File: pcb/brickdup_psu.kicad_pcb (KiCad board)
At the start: 2 copper layers, 32 x 18 mm, 24 parts, among them J1 VBAT/GND in, J2 5V/SENSE/GND, U1 MP9486A

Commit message: pcb: JST-PH connectors (J1/J2) + more LEMO clearance
Switch board I/O to JST-PH 2.0mm SMD side-entry connectors so the board is
plug-in/serviceable and stays single-side SMD for JLC:
- J1 (S2B-PH-SM4-TB): VBAT/GND from the LEMO (crimp cable = no solder).
- J2 (S3B-PH-SM4-TB): 5V/SENSE(GPIO7)/GND to the Heltec (pigtail; the Heltec's
  3 pads remain the one unavoidable solder point since it's a bare module).
Schematic/BOM/outline/render updated; ERC still electrically clean; gerbers OK.
Placement remains a rough GUI-arrange/route starting point.

Enclosure: add psu_gap_e (board east edge holdback) so J1 + its plug clear the
LEMO's rear cups. Clearance echo now reports 15.6 mm (was 12.6). Compiles clean.

Co-Authored-By: Claude Opus 4.8 <noreply@anthropic.com>
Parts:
- J1: value VBAT/GND in -> VBAT/GND (JST PH); footprint PinHeader_1x02_P2.54mm_Vertical -> JST_PH_S2B-PH-SM4-TB_1x02-1MP_P2.00mm_Horizontal
- J2: value 5V/SENSE/GND -> 5V/SENSE/GND (JST PH); footprint PinHeader_1x03_P2.54mm_Vertical -> JST_PH_S3B-PH-SM4-TB_1x03-1MP_P2.00mm_Horizontal
- moved J1 2.55 mm to (28.5, 13.0), turned to -90 degrees
- moved J2 1.58 mm to (6.00, 2.50)

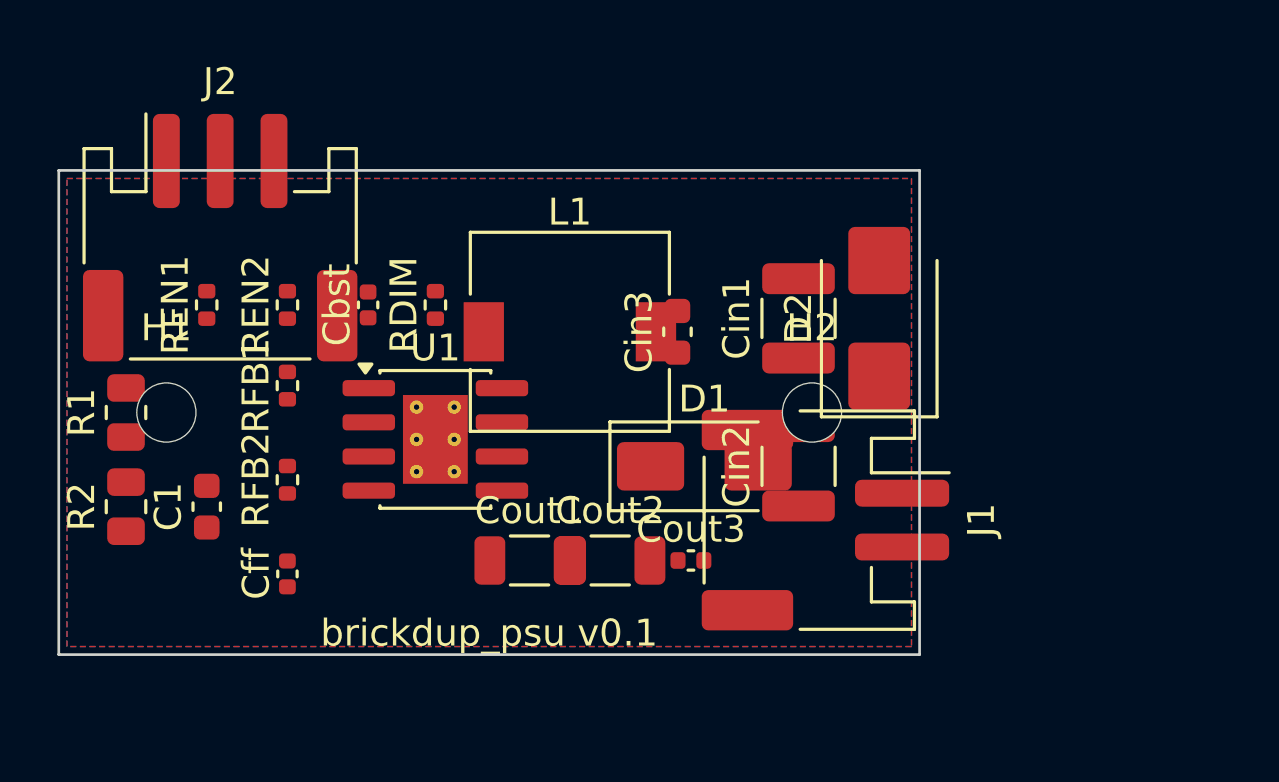
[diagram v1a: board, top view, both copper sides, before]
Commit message: pcb: enlarge board to 38x18 + diagonal corner holes for easier layout
Grow the board length-wise (32 -> 38 mm; width stays 18, set by the south
channel) for ~19% more area to spread parts, and move the two M2 mounting holes
to diagonal corners (NW 4,4 / SE 34,14) so the central band is free for the
regulator + input cluster. Net effect: much easier to arrange + route in the GUI.

Enclosure (node_enclosure.scad v11): psu_l 38, psu_holes as diagonal corner
pairs (bosses + pilots iterate the pair list). Outer box unchanged at
75.6 x 60.7 x 24.4 mm (length grew into the existing channel); LEMO clearance
still 15.6 mm. base/lid/both compile clean.

PCB: re-placed all 22 parts in functional zones using the freed centre; ERC
electrically clean, gerbers export. Placement still a rough GUI starting point.
Board outline SVG + README dims updated to 38x18 / corner holes.

Co-Authored-By: Claude Opus 4.8 <noreply@anthropic.com>
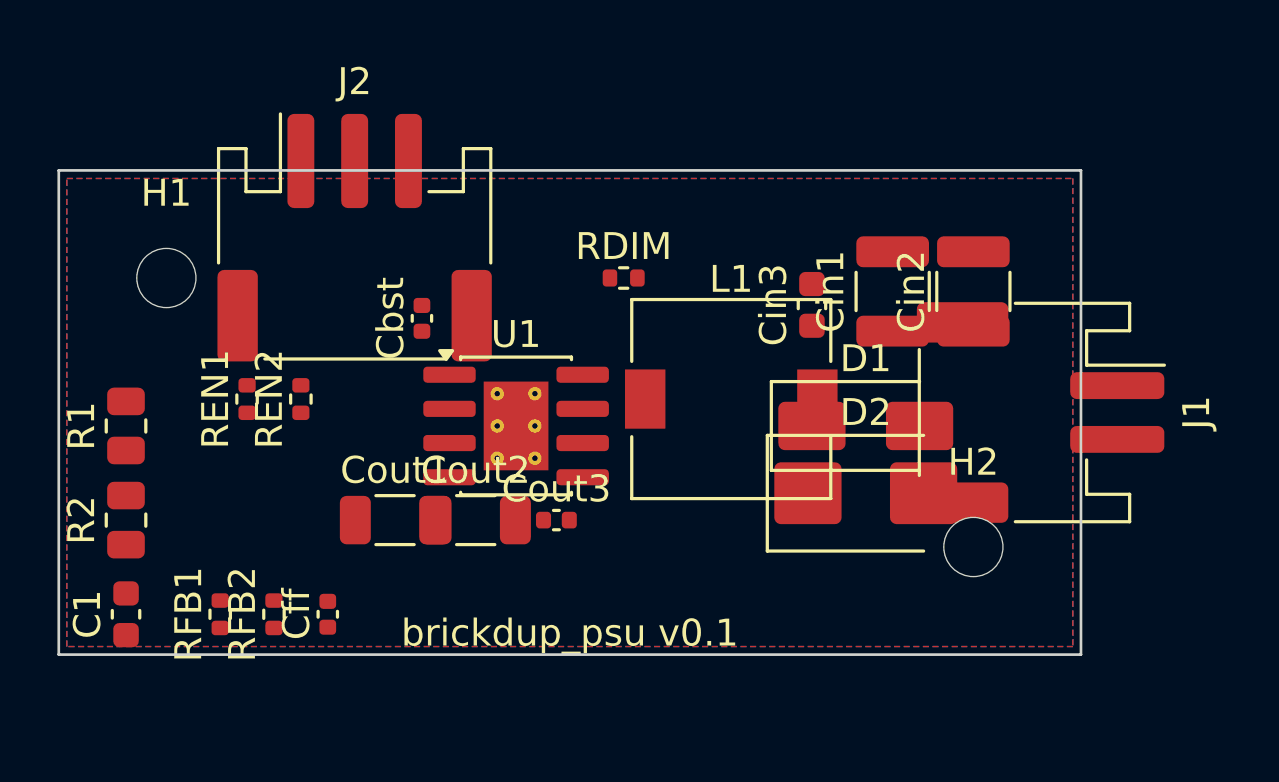
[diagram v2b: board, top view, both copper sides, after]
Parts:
- moved Cin2 9.19 mm to (34.0, 4.50)
- moved J1 8.94 mm to (36.5, 9.00)
- moved RFB1 8.86 mm to (6.00, 16.5)
- moved H2 7.81 mm to (34.0, 14.0)
- moved RDIM 7.07 mm to (21.0, 4.00), turned to 0 degrees
- moved D2 6.52 mm to (30.0, 12.0), turned to 0 degrees
- moved L1 6.50 mm to (25.0, 8.50)
- moved D1 6.18 mm to (30.0, 9.50)
- moved Cout1 5.22 mm to (12.5, 13.0)
- moved Cout2 5.22 mm to (15.5, 13.0)
- moved Cout3 5.22 mm to (18.5, 13.0)
- moved Cin3 5.10 mm to (28.0, 5.00)
- moved RFB2 5.02 mm to (8.00, 16.5)
- moved C1 5.00 mm to (2.50, 16.5)
- moved H1 5.00 mm to (4.00, 4.00)
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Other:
- board size 32 x 18 mm -> 38 x 18 mm

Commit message: pcb: 40x20 board + auto-spread placement (0 pad overlaps)
Enlarge to 40x20 mm and add a separation-solver placement (random-restart
relaxation using pad-bbox extents) that reaches 0 pad overlaps -- a clean,
manufacturable, routable starting board (previously parts sat on each other /
on the mounting holes). Mounting holes diagonal at (4,4) and (32,16); the SE
hole is pulled inboard so it clears the east-edge J1 connector. GND pours both
layers; value silk hidden, refs shrunk.

Enclosure v11: psu_l 40, psu_w 20, psu_holes (4,4)+(32,16). Outer grows to
~76 x 63 x 24 mm; LEMO clearance 15.1 mm. Compiles clean.

Routing is still to do (the 41 unconnected DRC items are the ratsnest). Docs +
board_outline.svg updated to 40x20.

Co-Authored-By: Claude Opus 4.8 <noreply@anthropic.com>
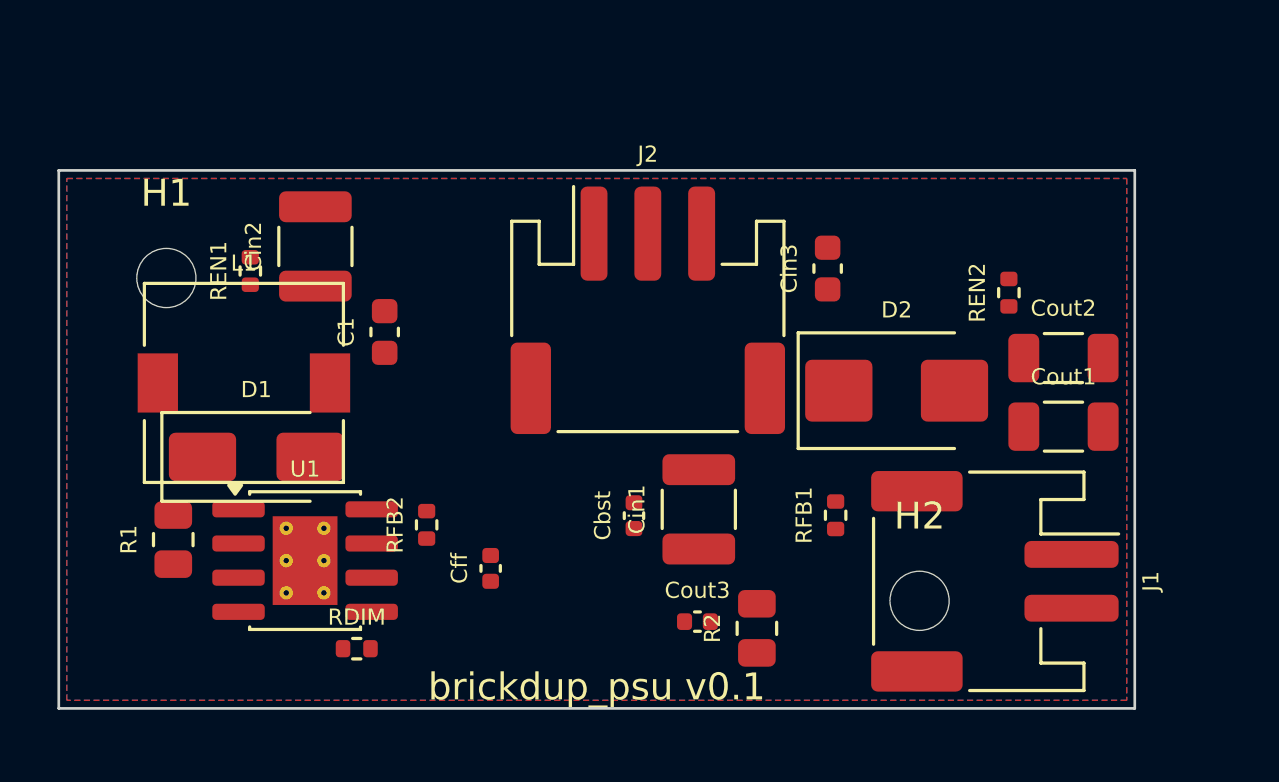
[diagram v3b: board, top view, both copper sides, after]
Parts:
- moved REN2 26.6 mm to (35.3, 4.55)
- moved Cout1 25.1 mm to (37.4, 9.53)
- moved Cin2 24.5 mm to (9.54, 2.83)
- moved R2 23.8 mm to (26.0, 17.0)
- moved RFB1 23.2 mm to (28.9, 12.8)
- moved D1 22.7 mm to (7.34, 10.6)
- moved Cout2 22.7 mm to (37.3, 6.98)
- moved L1 18.1 mm to (6.88, 7.90)
- moved RDIM 17.0 mm to (11.1, 17.8)
- moved C1 14.2 mm to (12.1, 6.01)
- moved J2 11.2 mm to (21.9, 5.20)
- moved Cin1 10.8 mm to (23.8, 12.6)
- moved Cbst 10.8 mm to (21.4, 12.8)
- moved U1 9.30 mm to (9.16, 14.5)
- moved RFB2 6.58 mm to (13.7, 13.2)
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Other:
- board size 38 x 18 mm -> 40 x 20 mm

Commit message: pcb: auto-route the board (freerouting) + JLCPCB fab outputs
Full scripted place-and-route pipeline, all reproducible:
  gen_kicad.py -> gen_pcb.py (separation-solver placement, 0 pad overlaps)
  -> export_dsn.py (zones stripped) -> freerouting v2 -> apply_route.py
  (import SES, normalize vias to 0.3/0.6, hide silk refs, fill GND pours).

Result: 40x20 2-layer board, fully placed and **fully routed** -- 0 unconnected,
0 shorts. U1 exposed pad tied to GND (added EP pin to the symbol; grounded by the
top pour). GND poured both layers; copper-to-edge rule 0.3 mm (JLC-safe).
Remaining DRC (~30) is cosmetic silk + a few courtyard/edge/thermal warnings,
documented in README sec 8 -- no opens/shorts.

Adds fab/ with gerbers + zip + CPL + BOM ready to upload to JLCPCB, a 3D render
(docs/pcb_routed_3d.png), and a beginner "Opening it in KiCad" guide.

Co-Authored-By: Claude Opus 4.8 <noreply@anthropic.com>
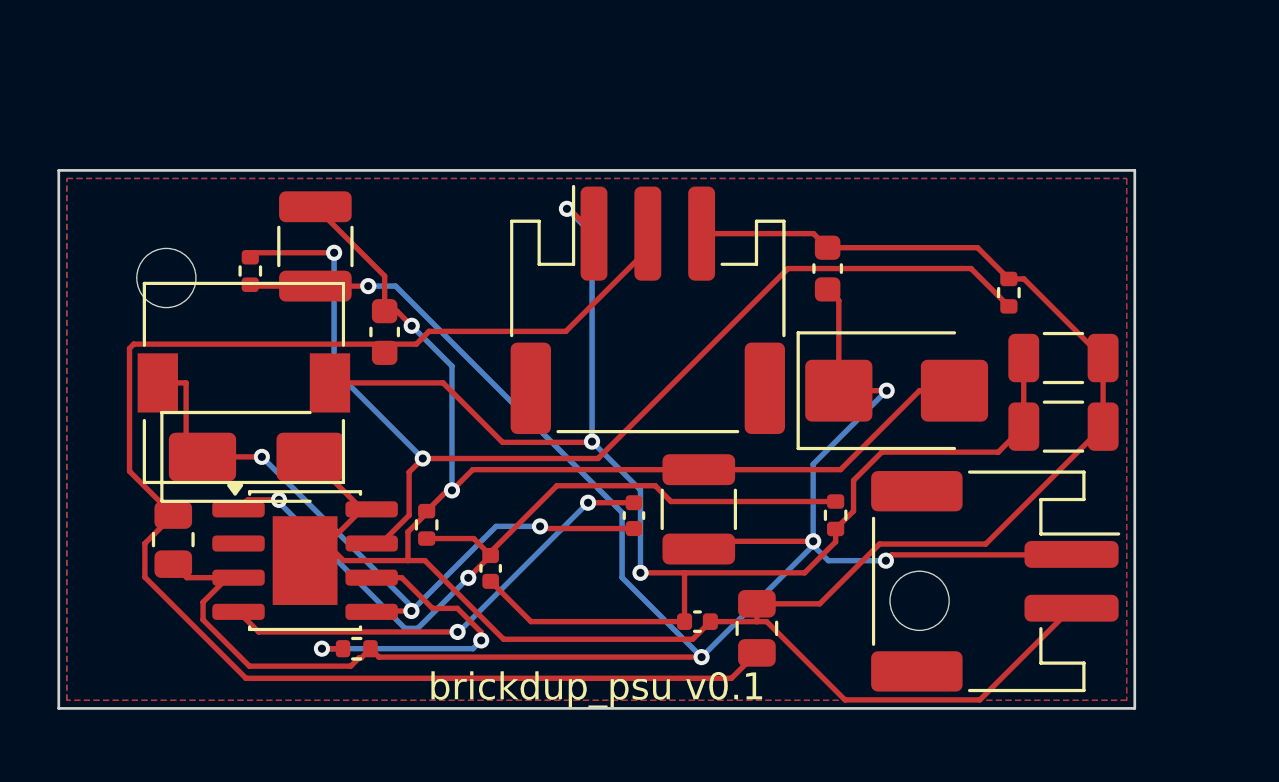
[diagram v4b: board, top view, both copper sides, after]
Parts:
- U1: footprint SOIC-8-1EP_3.9x4.9mm_P1.27mm_EP2.41x3.3mm_ThermalVias -> SOIC-8-1EP_3.9x4.9mm_P1.27mm_EP2.41x3.3mm
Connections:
- U1 pad 9: (no net) -> GND
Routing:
- net GND: track 0.00 -> 110.2 mm, vias 0 -> 2
- net VBAT: track 0.00 -> 81.3 mm, vias 0 -> 5
- net +5V: track 0.00 -> 56.4 mm, vias 0 -> 3
- net SENSE: track 0.00 -> 56.0 mm
- net EN: track 0.00 -> 41.6 mm, vias 0 -> 2
- net FB: track 0.00 -> 29.5 mm, vias 0 -> 2
- net SW: track 0.00 -> 25.4 mm, vias 0 -> 3
- net BST: track 0.00 -> 17.0 mm, vias 0 -> 2
- net DIM: track 0.00 -> 12.1 mm, vias 0 -> 2

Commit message: pcb: hot-loop tightening pass (better placement -> cleaner route)
Re-floorplan around the switcher's critical loops: U1 rotated so VIN/Cin cluster
toward the J1 input and SW/GND face the D1+L1 output side, FB divider by the FB
pin (off SW), sense divider clear of the SW node. Re-ran the place+route pipeline.

Result vs the previous route: still 0 unconnected / 0 shorts, and now also 0
copper-edge violations (was 3) with fewer vias (15 vs 21) = more direct loops.
DRC down to 20, all cosmetic silk + courtyard/thermal warnings. Regenerated
fab/ outputs + 3D render.

Co-Authored-By: Claude Opus 4.8 <noreply@anthropic.com>
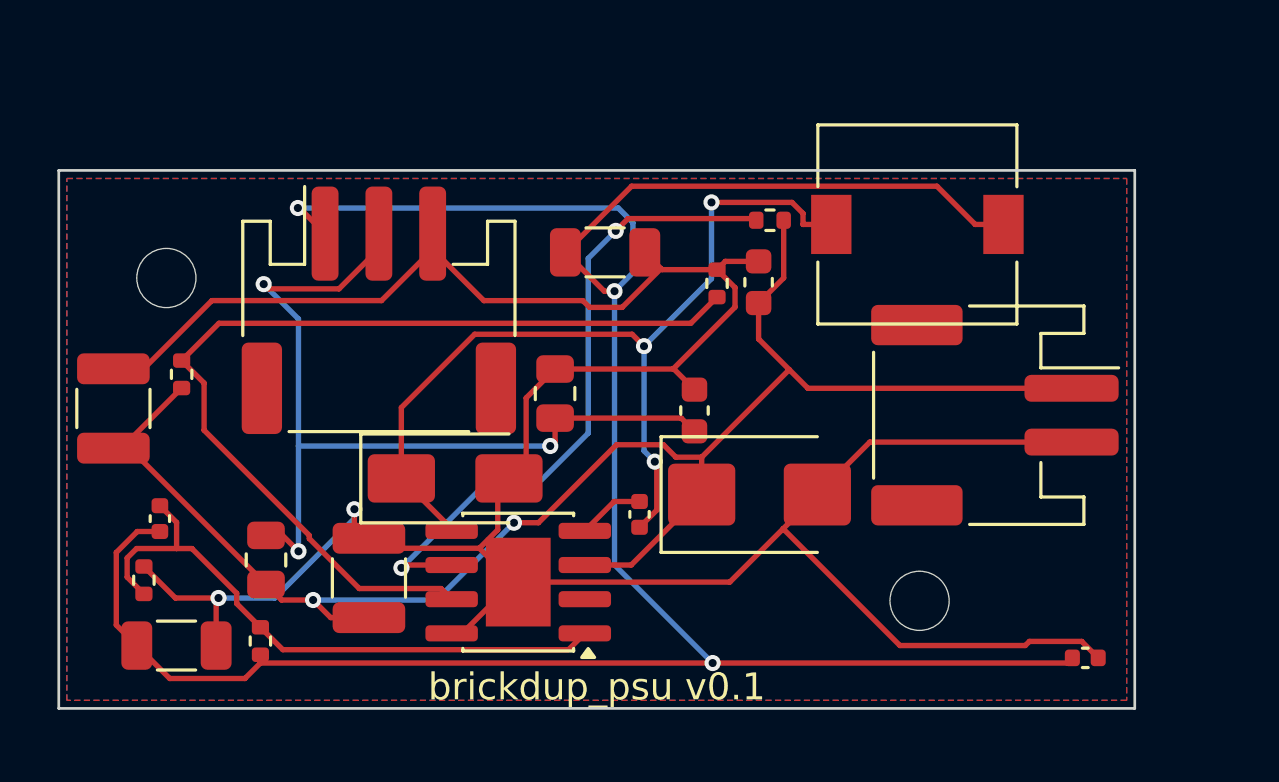
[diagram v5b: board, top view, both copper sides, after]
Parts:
- moved Cout1 34.0 mm to (4.38, 17.7)
- moved L1 25.7 mm to (31.9, 2.01)
- moved RDIM 22.1 mm to (26.4, 1.85)
- moved Cin1 22.1 mm to (2.03, 8.85)
- moved RFB1 21.9 mm to (7.50, 17.5)
- moved Cout2 17.5 mm to (20.3, 3.05)
- moved Cout3 14.5 mm to (38.2, 18.1)
- moved Cin2 12.5 mm to (11.5, 15.2)
- moved Cff 12.4 mm to (3.76, 12.9)
- moved C1 11.9 mm to (23.6, 8.93)
- moved R2 11.5 mm to (18.4, 8.30)
- moved REN2 10.9 mm to (24.5, 4.20)
- moved RFB2 10.7 mm to (3.16, 15.2)
- moved J2 10.00 mm to (11.9, 5.20)
- moved U1 7.96 mm to (17.1, 15.3), turned to 180 degrees
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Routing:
- net +5V: track 56.4 -> 94.2 mm
- net SENSE: track 56.0 -> 33.3 mm, vias 0 -> 3
- net VBAT: track 81.3 -> 60.8 mm, vias 5 -> 2
- net BST: track 17.0 -> 2.49 mm, vias 2 -> 0
- net DIM: track 12.1 -> 24.3 mm
- net SW: track 25.4 -> 34.3 mm
- net FB: track 29.5 -> 22.6 mm, vias 2 -> 0
- net EN: track 41.6 -> 35.7 mm, vias 2 -> 0
- net GND: track 110.2 -> 106.0 mm

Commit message: pcb: verify MP9486A pinout, tie DIM->EN, ngspice sims
Pre-fab validation pass:
- Pinout VERIFIED against the official MPS datasheet (1 FB, 2 NC, 3 VIN, 4 BST,
  5 SW, 6 DIM, 7 EN, 8 GND, EP->GND) -- matches the symbol/board.
- Datasheet fix: for a non-dimming buck, tie DIM(6) to EN(7). Done -- DIM merged
  into the EN net, the DNP RDIM pull-up removed (21 parts now).
- Re-ran place+route; cleared edge-hugging GND traces (pour carries GND) +
  stitched one re-islanded GND pad. Board: 0 unconnected, 0 shorts, 0 copper-edge;
  17 DRC left = 6 courtyard warnings + cosmetic silk.
- ngspice: divider DC sweep (GPIO7 1.66 V @16.8 V .. 2.50 V @25.2 V, matches math)
  and ideal-buck transient (IL peak ~1.30 A < 1.7 A Isat, dIL ~39%). True output
  ripple / loop stability still need MPSmart + bench (noted in README sec 9).

Regenerated fab/ + 3D render. README/BOM/schematic SVG updated.

Co-Authored-By: Claude Opus 4.8 <noreply@anthropic.com>
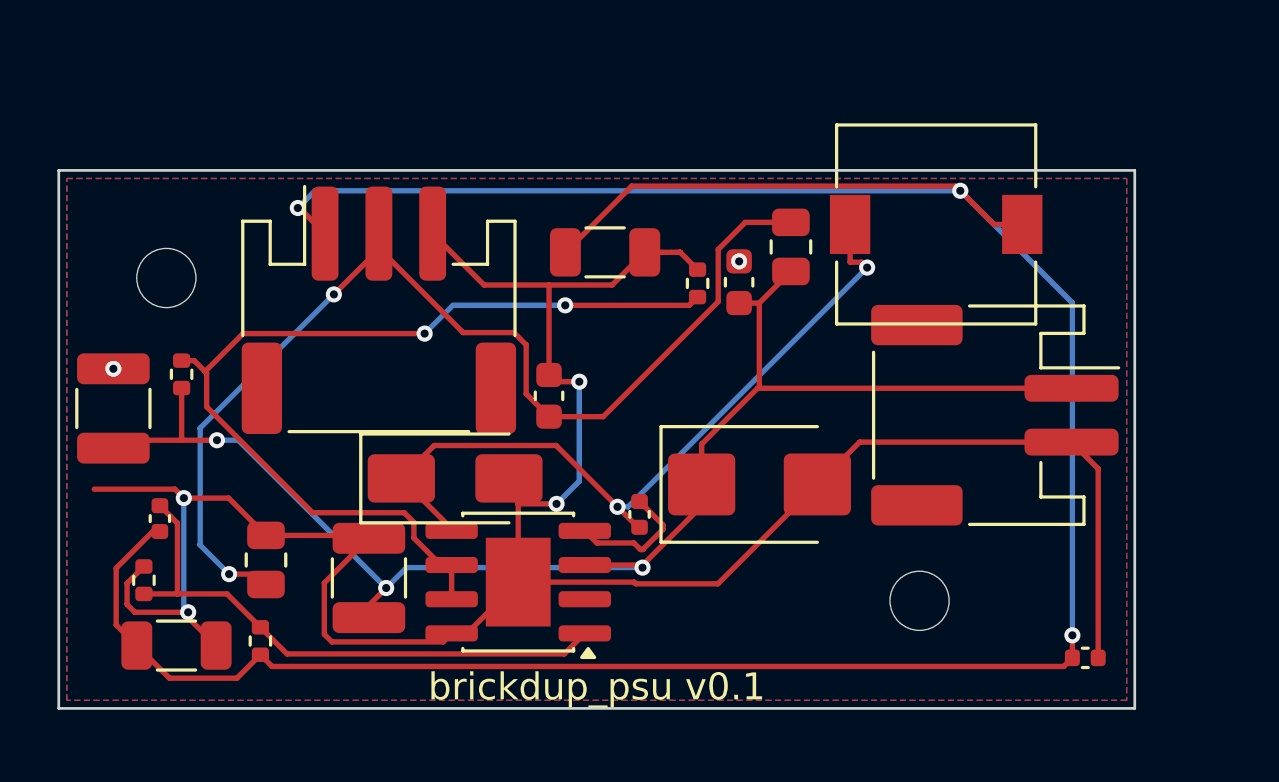
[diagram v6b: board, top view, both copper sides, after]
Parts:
- removed RDIM: DNP, R_0402_1005Metric
- moved R1 22.7 mm to (27.2, 2.84)
- moved R2 12.4 mm to (7.70, 14.5)
- moved C1 5.43 mm to (18.2, 8.38)
- moved REN2 0.72 mm to (23.7, 4.20)
- moved Cin3 0.72 mm to (25.3, 4.16)
- moved L1 0.70 mm to (32.6, 2.01)
- moved D2 0.38 mm to (26.1, 11.7)
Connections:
- U1 pad 6: DIM -> EN
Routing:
- net DIM: track 24.3 -> 0.00 mm, vias 2 -> 0
- net GND: track 106.0 -> 91.0 mm, vias 2 -> 6
- net +5V: track 94.2 -> 105.3 mm
- net VBAT: track 60.8 -> 53.5 mm, vias 2 -> 3
- net SENSE: track 33.3 -> 40.5 mm, vias 3 -> 2
- net SW: track 34.3 -> 28.4 mm, vias 3 -> 2
- net BST: track 2.49 -> 4.90 mm
- net FB: track 22.6 -> 21.2 mm
- net EN: track 35.7 -> 35.0 mm, vias 0 -> 2
